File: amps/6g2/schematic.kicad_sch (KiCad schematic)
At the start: 50 parts, among them T1 125P1A, T2 125A10B

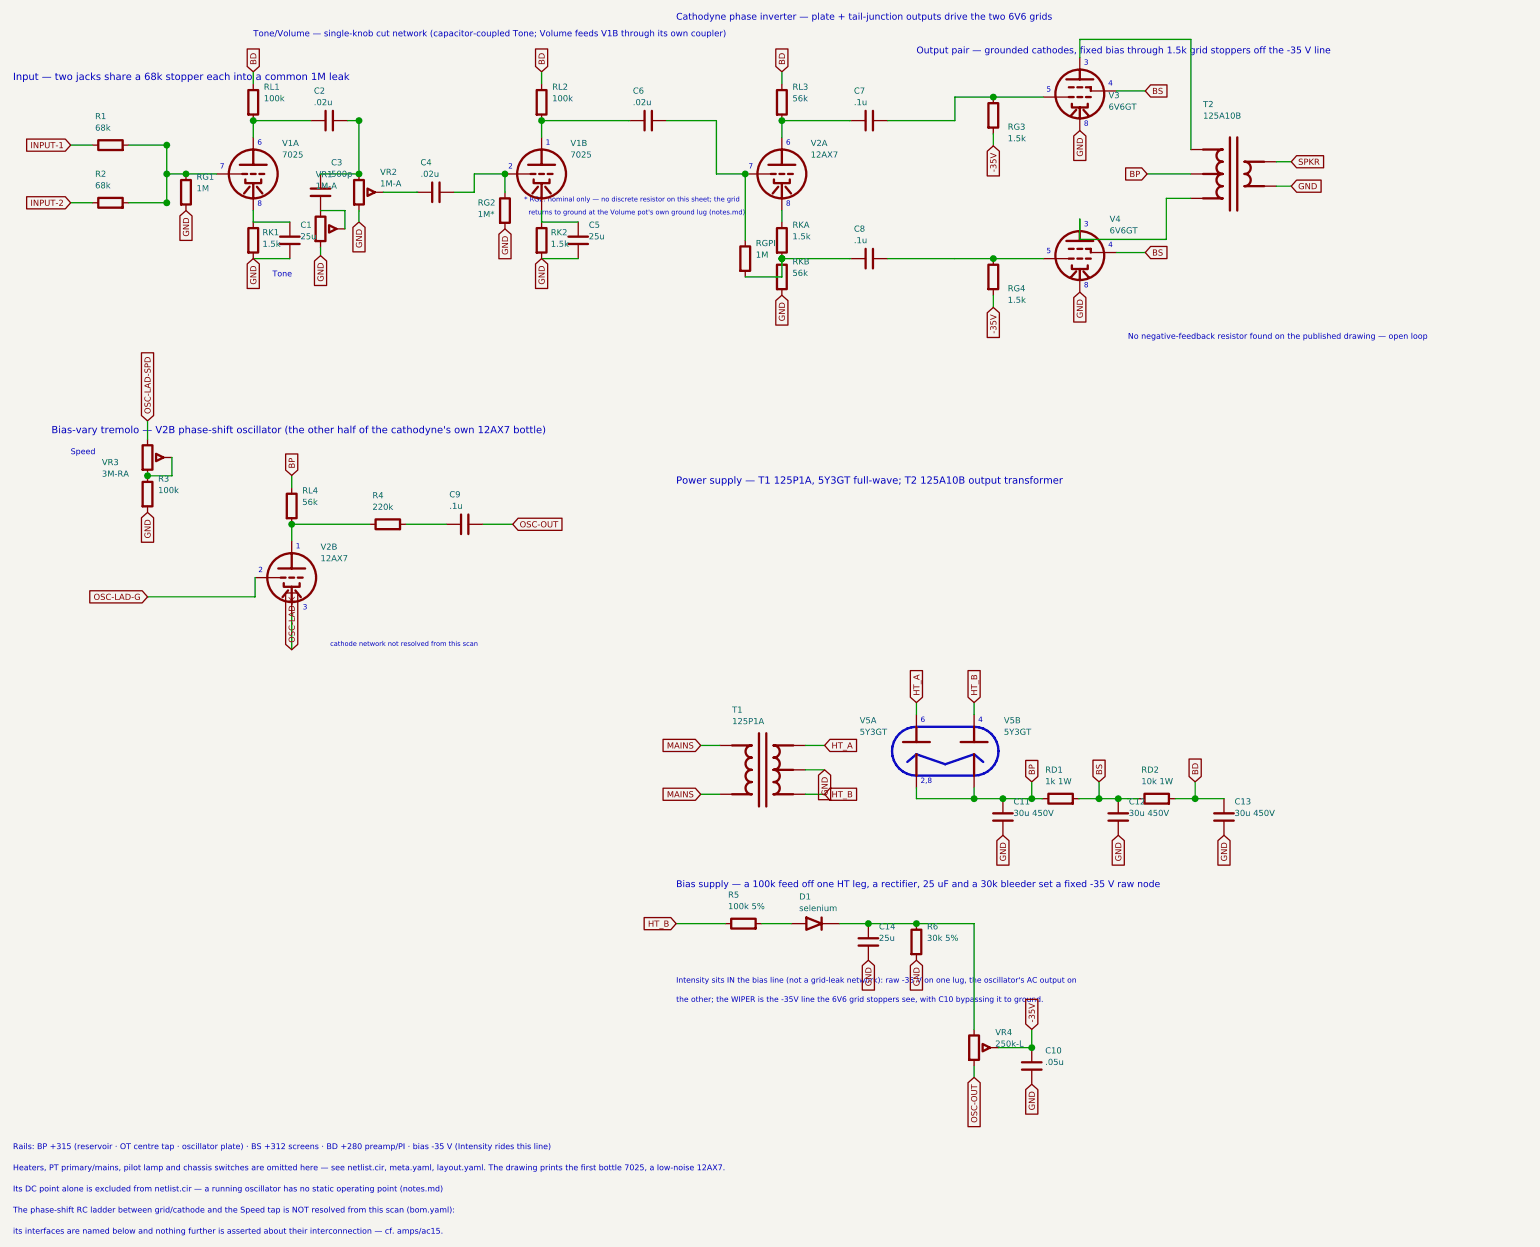
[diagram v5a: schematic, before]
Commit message: Fix: schematic sheet notes no longer name repository files
Thirty-seven committed sheets rendered footnotes and section notes such as
"Heaters and PT primary omitted — see netlist.cir and meta.yaml" or
"excluded from netlist.cir (notes.md)" to visitors through KiCanvas. The
prose sweeps never counted sheets. Rewritten in the site's own words — the
netlist, the sources list, the circuit story, the parts list, the board
drawing — in 59 strings across 33 draw scripts, keeping every technical
claim as it was; the three tone sheets (6G4, 6G5, 6G6-B) are under repair
elsewhere and keep theirs for now. The sweep touched only strings passed to
the sheet's note, text, caption and footnote calls, never a path or a value.

Gates: check_schematics 40/0, connectivity 0 isolated pins;
verify_schematic_nets 40 clean; only the regenerated sheets and their served
copies changed.

Co-Authored-By: Claude Fable 5.1 <noreply@anthropic.com>
Claude-Session: https://claude.ai/code/session_01KBMfdh37HmCL2iWcBiL5J1
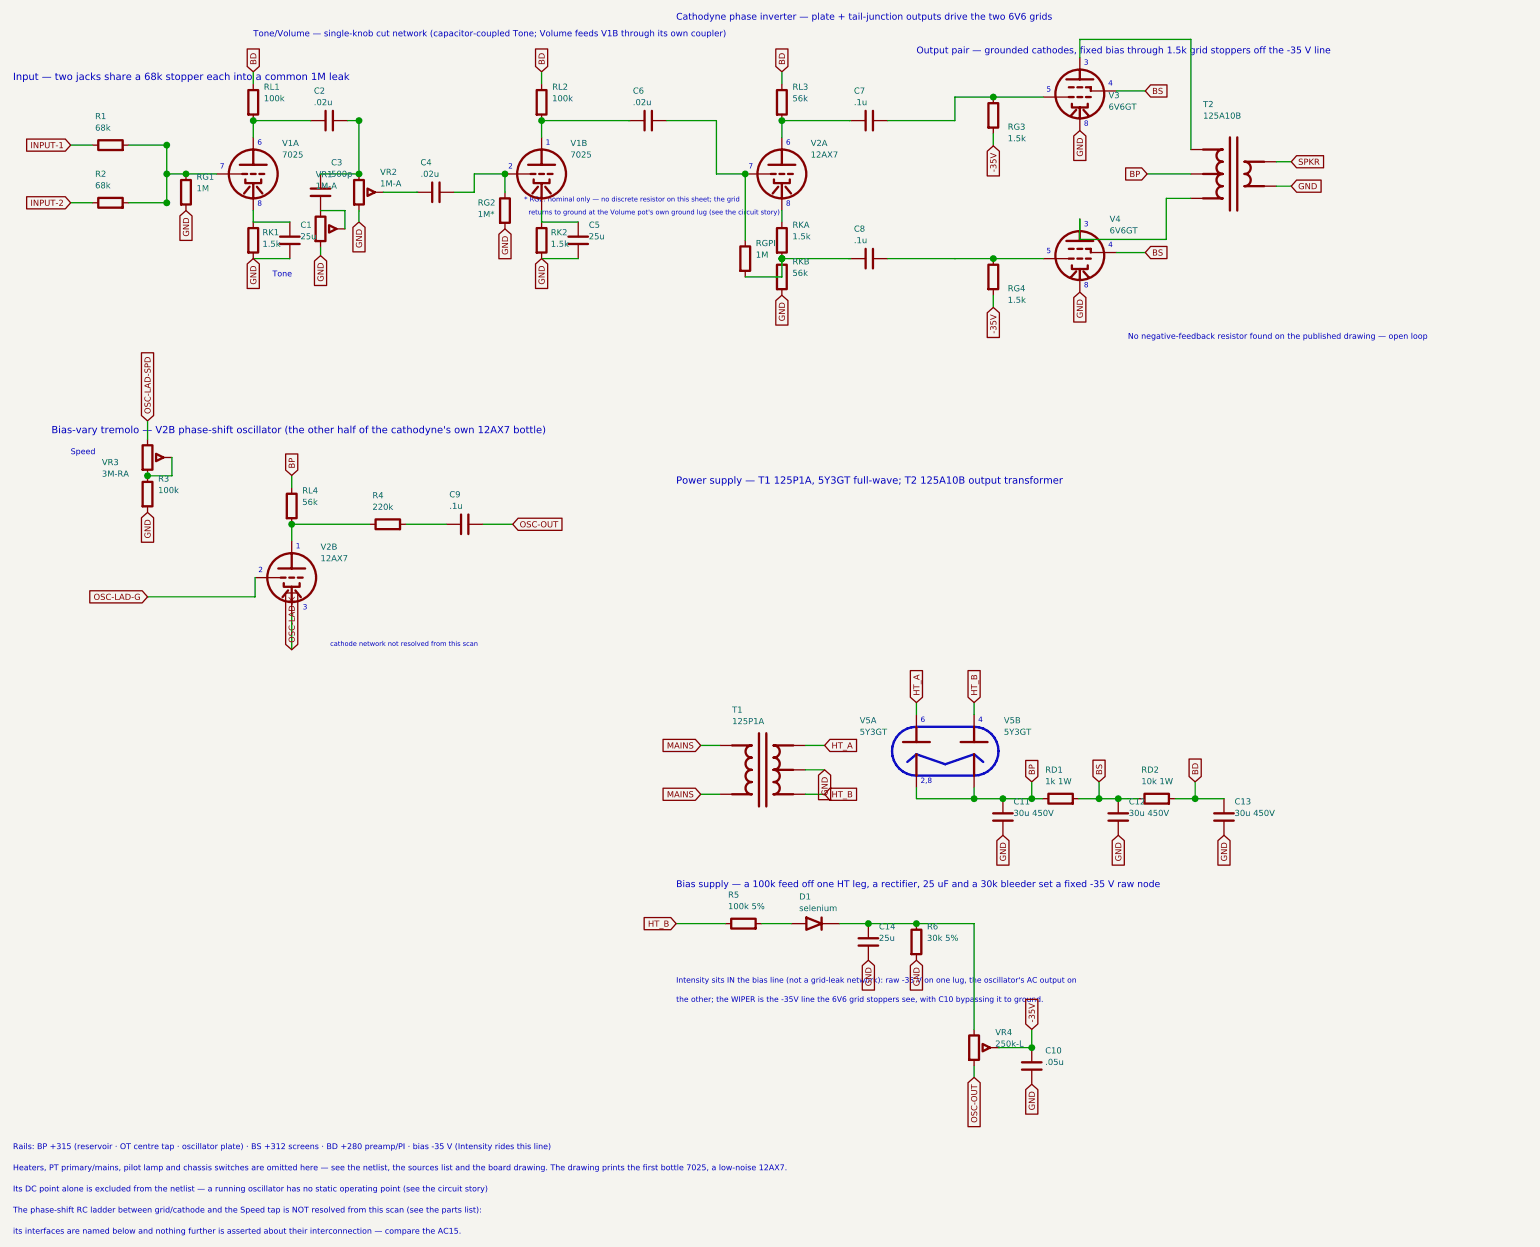
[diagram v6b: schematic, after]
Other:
- note added: "Heaters, PT primary/mains, pilot lamp and chassis switches are omitted here — see the netlist, the sources list and the board drawing. The drawing prints the first bottle 7025, a low-noise 12AX7."
- note added: "Its DC point alone is excluded from the netlist — a running oscillator has no static operating point (see the circuit story)"
- note added: "The phase-shift RC ladder between grid/cathode and the Speed tap is NOT resolved from this scan (see the parts list):"
- note added: "its interfaces are named below and nothing further is asserted about their interconnection — compare the AC15."
- note added: "returns to ground at the Volume pot's own ground lug (see the circuit story)"
- note removed: "Heaters, PT primary/mains, pilot lamp and chassis switches are omitted here — see netlist.cir, meta.yaml, layout.yaml. The drawing prints the first bottle 7025, a low-noise 12AX7."
- note removed: "Its DC point alone is excluded from netlist.cir — a running oscillator has no static operating point (notes.md)"
- note removed: "The phase-shift RC ladder between grid/cathode and the Speed tap is NOT resolved from this scan (bom.yaml):"
- note removed: "its interfaces are named below and nothing further is asserted about their interconnection — cf. amps/ac15."
- note removed: "returns to ground at the Volume pot's own ground lug (notes.md)"
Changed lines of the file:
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@@
   (text "* RG2: nominal only — no discrete resistor on this sheet; the grid" (at 119.08 51.68 0)
     (effects (font (size 1 1)) (justify left)))
-  (text "  returns to ground at the Volume pot's own ground lug (notes.md)" (at 119.08 54.38 0)
+  (text "  returns to ground at the Volume pot's own ground lug (see the circuit story)" (at 119.08 54.38 0)
     (effects (font (size 1 1)) (justify left)))
   (wire (pts (xy 122.7 53.8) (xy 122.7 56.18))
@@
   (text "Rails: BP +315 (reservoir · OT centre tap · oscillator plate) · BS +312 screens · BD +280 preamp/PI · bias -35 V (Intensity rides this line)" (at 12.7 248.792 0)
     (effects (font (size 1.2 1.2)) (justify left)))
-  (text "Heaters, PT primary/mains, pilot lamp and chassis switches are omitted here — see netlist.cir, meta.yaml, layout.yaml. The drawing prints the first bottle 7025, a low-noise 12AX7." (at 12.7 253.192 0)
-    (effects (font (size 1.2 1.2)) (justify left)))
-  (text "Its DC point alone is excluded from netlist.cir — a running oscillator has no static operating point (notes.md)" (at 12.7 257.592 0)
-    (effects (font (size 1.2 1.2)) (justify left)))
-  (text "The phase-shift RC ladder between grid/cathode and the Speed tap is NOT resolved from this scan (bom.yaml):" (at 12.7 261.992 0)
-    (effects (font (size 1.2 1.2)) (justify left)))
-  (text "its interfaces are named below and nothing further is asserted about their interconnection — cf. amps/ac15." (at 12.7 266.392 0)
+  (text "Heaters, PT primary/mains, pilot lamp and chassis switches are omitted here — see the netlist, the sources list and the board drawing. The drawing prints the first bottle 7025, a low-noise 12AX7." (at 12.7 253.192 0)
+    (effects (font (size 1.2 1.2)) (justify left)))
+  (text "Its DC point alone is excluded from the netlist — a running oscillator has no static operating point (see the circuit story)" (at 12.7 257.592 0)
+    (effects (font (size 1.2 1.2)) (justify left)))
+  (text "The phase-shift RC ladder between grid/cathode and the Speed tap is NOT resolved from this scan (see the parts list):" (at 12.7 261.992 0)
+    (effects (font (size 1.2 1.2)) (justify left)))
+  (text "its interfaces are named below and nothing further is asserted about their interconnection — compare the AC15." (at 12.7 266.392 0)
     (effects (font (size 1.2 1.2)) (justify left)))
   (sheet_instances (path "/" (page "1")))

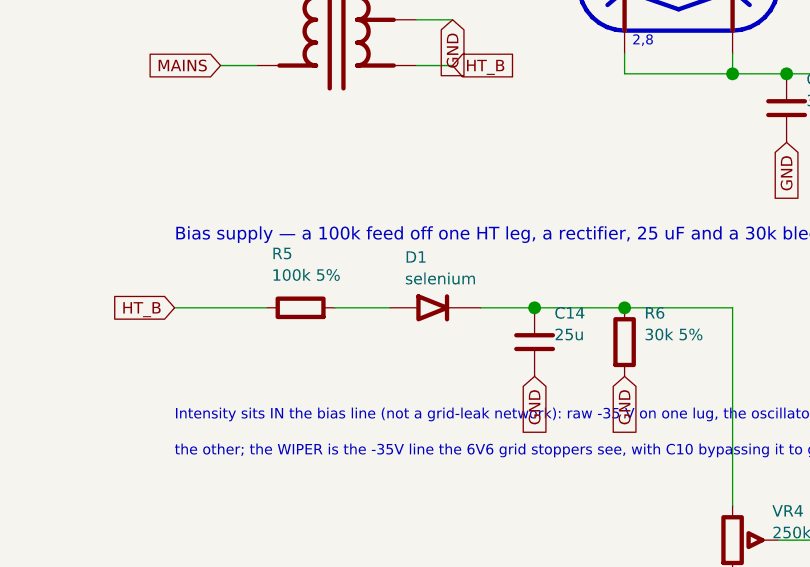
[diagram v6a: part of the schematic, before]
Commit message: Fix: 17 bias rectifiers and six HT diodes drawn backwards; the 6G6-B and 6G4 bias rows as their drawings show; AA1164 V4 units
Rectifier polarity has no gate. The netlists model every supply as an ideal
source, the sheet-vs-board check treats a two-terminal part as unordered, and
the boards' `cathode:` fields were copied from the sheets. Measured over all
68 diodes on 40 sheets: 18 negative-bias rectifiers had the cathode on the
negative node (a diode that way round would charge the node POSITIVE), and all
six 6G6-B HT diodes pointed away from B+. The printed negative bias on each of
those sheets falsifies the drawn orientation; the nine bias rectifiers already
right (AA1164, AA864, AB165, B15N, DR103, JTM100, M1959, M2204, 6G6-B) show
the idiom. Flipped: 5E4-A, 5E5-A, 5E6-A, 5F10, 5F4, 5F6, 5F6-A, 5F8-A, 5G9,
6G2, 6G3, 6G4, 6G5, AA964, AB763, AB763 Super, AB763 Twin, JTM45 (the
M1987's is with the Marshall board repair) and the 6G6-B's DR1-DR6. The
5F8-A board, which had copied its sheet, has the band moved to the tap side;
the other boards' bands are with the board-repair wave. A gate is next.

6G6-B bias. E-FB (6431x3364): the 1K 1W rises from TR1's SECOND secondary
terminal, a bias tap between the upper HT end and the grounded centre tap,
to the diode's + end. The sheet fed the diode from the HT end with the 1K
after it. T1 now carries its tap pin and the row reads tap -> 1K -> diode ->
-54 V. (The triage had read "HT end"; the native crop shows the tap.)

6G4 bias. A-FJ, read natively: tap -> rectifier -> 8 uF -> 10K -> the -55 V
node, which carries a second 8 uF and the 56K to ground as a bleeder. The
sheet fed the rectifier from an HT end, drew the 56K in series and carried
one capacitor. CBIAS2 joins the parts list, and RBIAS1's role now says
bleeder.

AA1164 V4. The K-FD sheet prints the phase inverter 7/6/8 and the tremolo
oscillator 2/1/3 (5554x4346); the sheet had them the other way round.

Gates: check_schematics 40/0 (+selftest), verify_schematic_nets 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
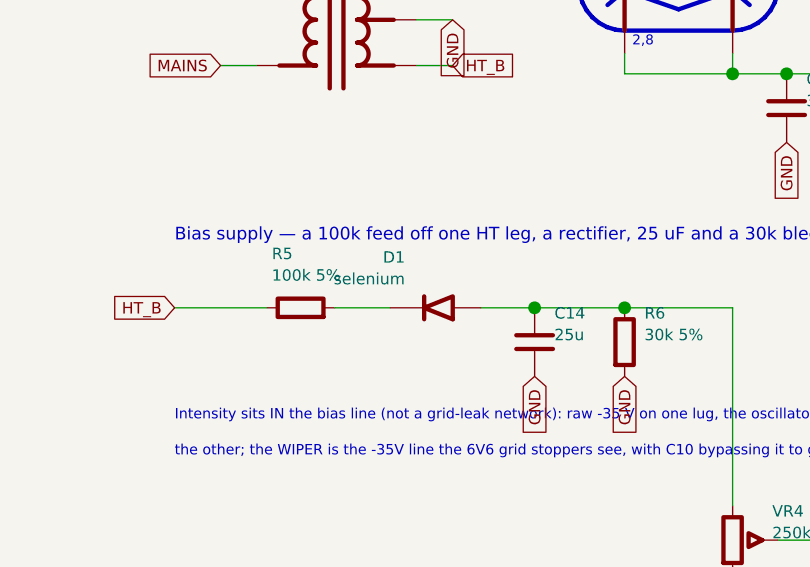
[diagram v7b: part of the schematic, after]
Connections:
- net at R5.2: now also D1.2 (K); no longer D1.1 (A)
- net at C14.1, R6.1, VR4.1: now also D1.1 (A); no longer D1.2 (K)
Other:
- moved on the sheet: D1
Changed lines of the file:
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@@
   (wire (pts (xy 168.51 202.18) (xy 174.62 202.18))
     (stroke (width 0) (type default)))
-  (symbol (lib_id "cx:DIODE_SS") (at 179.7 202.18 0) (unit 1)
+  (symbol (lib_id "cx:DIODE_SS") (at 179.7 202.18 180) (unit 1)
     (in_bom yes) (on_board yes)
     (property "Reference" "D1" (at 176.3 196.58 0) (effects (font (size 1.27 1.27)) (justify left)))

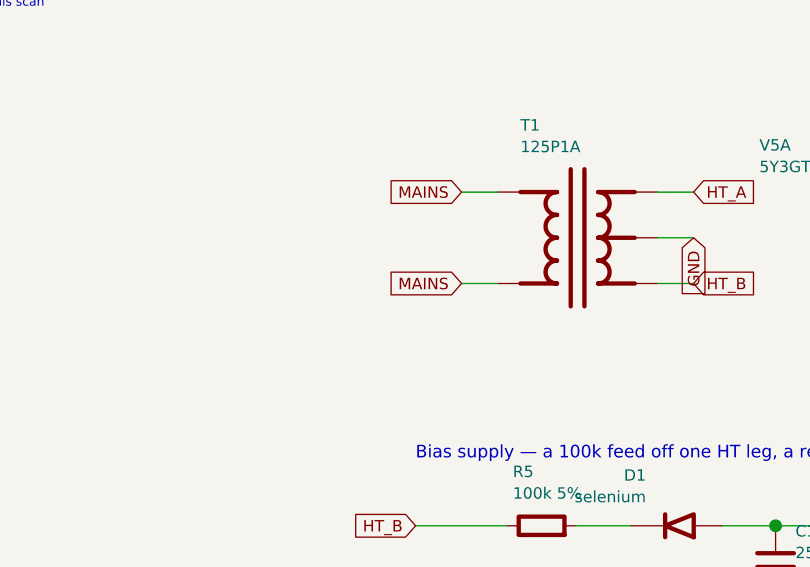
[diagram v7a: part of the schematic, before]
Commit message: Fix: the 6G5's rectifier was connected to nothing; 17 sheets shorted the mains by naming both leads alike
6G5 power supply. The sheet drew four diodes as a "silicon bridge" whose
HT_A/HT_B labels stopped 6 mm short of their wires. D1/D2's anodes sat on
the tremolo's cathode node (a tremolo wire's end touched the old diode
stub), D3/D4 ran from ground to the reservoir, and TR1's centre tap floated
under an open-pin waiver whose stated reason was the bridge itself.
A-FJ (Schematic Heaven 2153x1437, read enlarged): each HT end of TR1 runs
through a leg of three silicon diodes, every + (cathode) toward the +460 V
reservoir; the centre tap is grounded; TR1's second secondary terminal is a
bias tap feeding the 6G4's network part for part: rectifier, 8-150, 10K,
then 8-150 and a 56K bleeder at the -55 V line. Redrawn as the drawing
shows: D1-D6, TR1 with its tap pin, the centre tap to ground, the bias
network (CBIAS 25 uF -> 8 uF; RBIAS2, CBIAS2, RBIAS1 added), the waiver
deleted, and the notes, meta, netlist header and parts list no longer say
bridge. Not yet carried: the drawing's second 20-600 at the reservoir and
the standby switch (this sheet omits chassis switches by its own note);
and the tremolo ladder still runs through the transformer's corner of the
sheet, a layout clash rather than a connection, queued for its own redraw.

Mains. Two global labels with one name are one net. 16 of 24 power
transformers on the sheets carried a label named MAINS on both primary
leads, so the winding's two pins were one net: 5E4-A, 5E5-A, 5F4, 5G9,
6161, 6G2, 6G3, 6G4, AA1164, AA764, AA764-Vibro, AA964, AB763, AB763
Super, AB763 Twin, GA-40. The 6G5's loop ran from one MAINS label through
switch, fuse and winding back to the same name. No gate models the primary,
so a copy-pasted idiom did this. The second lead is now MAINS N, the AC15's
idiom; the AA1164's and AA964's second AC row, drawn under the first row's
name, is the neutral. The death and across-the-line caps stay on the le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
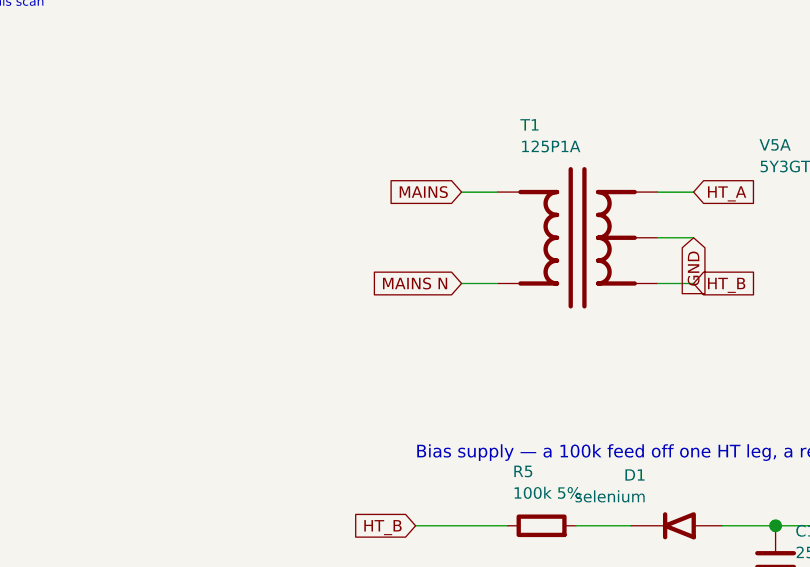
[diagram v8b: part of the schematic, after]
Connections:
- net MAINS: no longer T1.2 (PRI_2)
- new net MAINS N: T1.2 (PRI_2)
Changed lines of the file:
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@@
   (wire (pts (xy 159.81 175.26) (xy 155.81 175.26))
     (stroke (width 0) (type default)))
-  (global_label "MAINS" (shape input) (at 155.81 175.26 180)
+  (global_label "MAINS N" (shape input) (at 155.81 175.26 180)
     (effects (font (size 1.27 1.27)) (justify right)))
   (wire (pts (xy 177.59 165.1) (xy 181.59 165.1))
